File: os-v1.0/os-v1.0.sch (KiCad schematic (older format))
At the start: 53 parts, among them J1 Conn_01x02, J2 Conn_01x04, Q1 2N7002, SW1 SW_Push, SW2 SW_Push, SW3 SW_Push, SW4 SW_Push, SW5 SW_Push, U1 DS3231MZ, U10 MCP1812AT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

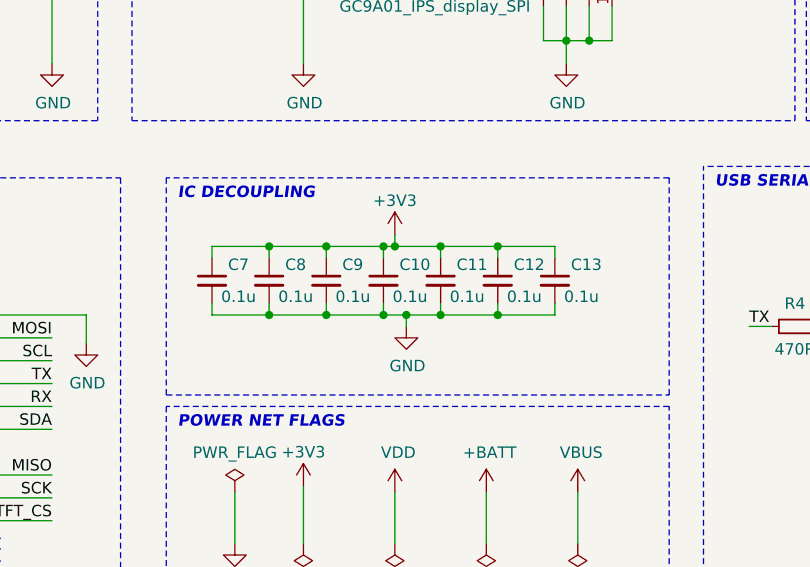
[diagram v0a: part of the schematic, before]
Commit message: adds addl cap to ch240e and updates board and bom
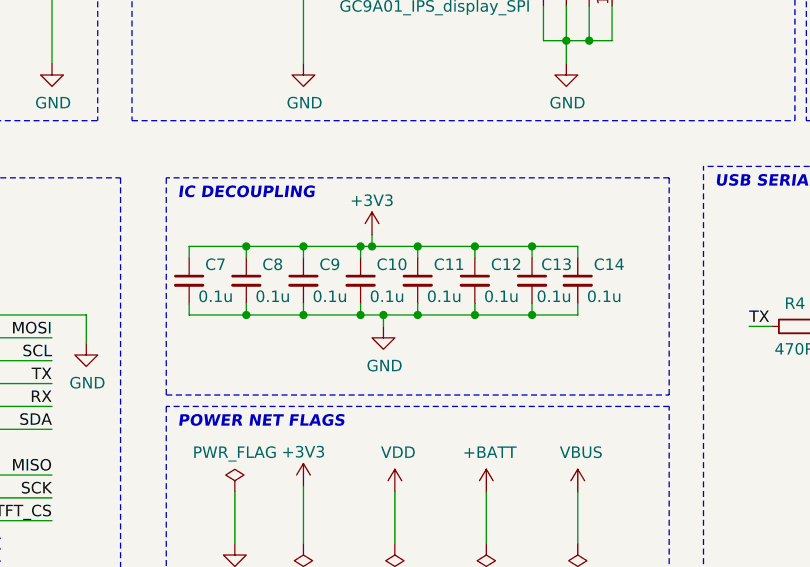
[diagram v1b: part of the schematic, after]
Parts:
- added C14: 0.1u, Capacitor_SMD:C_0603_1608Metric, symbol Device:C_Small
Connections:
- net +3V3: now also C14.1
- net GND: now also C14.2
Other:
- moved on the sheet: C10, C11, C12, C13, C7, C8, C9
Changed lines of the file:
@@
 Comment1 ""
 Comment2 ""
-Comment3 "Add 0.1u decoupling capacitor to Vcc/Vdd for U1-U3,U6"
+Comment3 "Add 0.1u decoupling capacitor to each Vcc/Vdd pin on U1-U3,U6"
 Comment4 "All resistors and capacitors are 0603 unless otherwise noted"
 $EndDescr
@@
 L power:GND #PWR057
 U 1 1 5F641A31
-P 6850 3350
-F 0 "#PWR057" H 6850 3100 50  0001 C CNN
-F 1 "GND" H 6855 3177 50  0000 C CNN
-F 2 "" H 6850 3350 50  0001 C CNN
-F 3 "" H 6850 3350 50  0001 C CNN
-	1    6850 3350
+P 6750 3350
+F 0 "#PWR057" H 6750 3100 50  0001 C CNN
+F 1 "GND" H 6755 3177 50  0000 C CNN
+F 2 "" H 6750 3350 50  0001 C CNN
+F 3 "" H 6750 3350 50  0001 C CNN
+	1    6750 3350
 	1    0    0    -1
 $EndComp
@@
 L Device:C_Small C9
 U 1 1 5F753E14
-P 6500 3150
-F 0 "C9" H 6570 3220 50  0000 L CNN
-F 1 "0.1u" H 6540 3080 50  0000 L CNN
-F 2 "Capacitor_SMD:C_0603_1608Metric" H 6500 3150 50  0001 C CNN
-F 3 "~" H 6500 3150 50  0001 C CNN
-	1    6500 3150
+P 6400 3150
+F 0 "C9" H 6470 3220 50  0000 L CNN
+F 1 "0.1u" H 6440 3080 50  0000 L CNN
+F 2 "Capacitor_SMD:C_0603_1608Metric" H 6400 3150 50  0001 C CNN
+F 3 "~" H 6400 3150 50  0001 C CNN
+	1    6400 3150
 	1    0    0    -1
 $EndComp
@@
 L Device:C_Small C10
 U 1 1 5F827434
-P 6750 3150
-F 0 "C10" H 6820 3220 50  0000 L CNN
-F 1 "0.1u" H 6790 3080 50  0000 L CNN
-F 2 "Capacitor_SMD:C_0603_1608Metric" H 6750 3150 50  0001 C CNN
-F 3 "~" H 6750 3150 50  0001 C CNN
-	1    6750 3150
+P 6650 3150
+F 0 "C10" H 6720 3220 50  0000 L CNN
+F 1 "0.1u" H 6690 3080 50  0000 L CNN
+F 2 "Capacitor_SMD:C_0603_1608Metric" H 6650 3150 50  0001 C CNN
+F 3 "~" H 6650 3150 50  0001 C CNN
+	1    6650 3150
 	1    0    0    -1
 $EndComp
@@
 L Device:C_Small C11
 U 1 1 5F8276CE
-P 7000 3150
-F 0 "C11" H 7070 3220 50  0000 L CNN
-F 1 "0.1u" H 7040 3080 50  0000 L CNN
-F 2 "Capacitor_SMD:C_0603_1608Metric" H 7000 3150 50  0001 C CNN
-F 3 "~" H 7000 3150 50  0001 C CNN
-	1    7000 3150
+P 6900 3150
+F 0 "C11" H 6970 3220 50  0000 L CNN
+F 1 "0.1u" H 6940 3080 50  0000 L CNN
+F 2 "Capacitor_SMD:C_0603_1608Metric" H 6900 3150 50  0001 C CNN
+F 3 "~" H 6900 3150 50  0001 C CNN
+	1    6900 3150
 	1    0    0    -1
 $EndComp
@@
 L Device:C_Small C12
 U 1 1 5F828FE0
-P 7250 3150
-F 0 "C12" H 7320 3220 50  0000 L CNN
-F 1 "0.1u" H 7290 3080 50  0000 L CNN
-F 2 "Capacitor_SMD:C_0603_1608Metric" H 7250 3150 50  0001 C CNN
-F 3 "~" H 7250 3150 50  0001 C CNN
-	1    7250 3150
+P 7150 3150
+F 0 "C12" H 7220 3220 50  0000 L CNN
+F 1 "0.1u" H 7190 3080 50  0000 L CNN
+F 2 "Capacitor_SMD:C_0603_1608Metric" H 7150 3150 50  0001 C CNN
+F 3 "~" H 7150 3150 50  0001 C CNN
+	1    7150 3150
 	1    0    0    -1
 $EndComp
@@
 L Device:C_Small C13
 U 1 1 5F8293A4
-P 7500 3150
-F 0 "C13" H 7570 3220 50  0000 L CNN
-F 1 "0.1u" H 7540 3080 50  0000 L CNN
-F 2 "Capacitor_SMD:C_0603_1608Metric" H 7500 3150 50  0001 C CNN
-F 3 "~" H 7500 3150 50  0001 C CNN
-	1    7500 3150
+P 7400 3150
+F 0 "C13" H 7440 3220 50  0000 L CNN
+F 1 "0.1u" H 7420 3080 50  0000 L CNN
+F 2 "Capacitor_SMD:C_0603_1608Metric" H 7400 3150 50  0001 C CNN
+F 3 "~" H 7400 3150 50  0001 C CNN
+	1    7400 3150
 	1    0    0    -1
 $EndComp
@@
 L Device:C_Small C8
 U 1 1 5F82A290
-P 6250 3150
-F 0 "C8" H 6320 3220 50  0000 L CNN
-F 1 "0.1u" H 6290 3080 50  0000 L CNN
-F 2 "Capacitor_SMD:C_0603_1608Metric" H 6250 3150 50  0001 C CNN
-F 3 "~" H 6250 3150 50  0001 C CNN
-	1    6250 3150
+P 6150 3150
+F 0 "C8" H 6220 3220 50  0000 L CNN
+F 1 "0.1u" H 6190 3080 50  0000 L CNN
+F 2 "Capacitor_SMD:C_0603_1608Metric" H 6150 3150 50  0001 C CNN
+F 3 "~" H 6150 3150 50  0001 C CNN
+	1    6150 3150
 	1    0    0    -1
 $EndComp
@@
 L Device:C_Small C7
 U 1 1 5F82A534
-P 6000 3150
-F 0 "C7" H 6070 3220 50  0000 L CNN
-F 1 "0.1u" H 6040 3080 50  0000 L CNN
-F 2 "Capacitor_SMD:C_0603_1608Metric" H 6000 3150 50  0001 C CNN
-F 3 "~" H 6000 3150 50  0001 C CNN
-	1    6000 3150
+P 5900 3150
+F 0 "C7" H 5970 3220 50  0000 L CNN
+F 1 "0.1u" H 5940 3080 50  0000 L CNN
+F 2 "Capacitor_SMD:C_0603_1608Metric" H 5900 3150 50  0001 C CNN
+F 3 "~" H 5900 3150 50  0001 C CNN
+	1    5900 3150
 	1    0    0    -1
 $EndComp
@@
 L power:+3V3 #PWR056
 U 1 1 5F890CE1
-P 6800 2950
-F 0 "#PWR056" H 6800 2800 50  0001 C CNN
-F 1 "+3V3" H 6800 3100 50  0000 C CNN
-F 2 "" H 6800 2950 50  0001 C CNN
-F 3 "" H 6800 2950 50  0001 C CNN
-	1    6800 2950
+P 6700 2950
+F 0 "#PWR056" H 6700 2800 50  0001 C CNN
+F 1 "+3V3" H 6700 3100 50  0000 C CNN
+F 2 "" H 6700 2950 50  0001 C CNN
+F 3 "" H 6700 2950 50  0001 C CNN
+	1    6700 2950
 	1    0    0    -1
 $EndComp
@@
 $EndComp
 Wire Wire Line
-	6000 3250 6000 3300
-Wire Wire Line
-	6000 3300 6250 3300
-Wire Wire Line
-	6250 3300 6250 3250
-Wire Wire Line
-	6250 3300 6500 3300
-Wire Wire Line
-	6500 3300 6500 3250
-Connection ~ 6250 3300
-Wire Wire Line
-	6500 3300 6750 3300
-Connection ~ 6500 3300
-Connection ~ 6850 3300
-Wire Wire Line
-	6850 3300 6850 3350
-Wire Wire Line
-	6850 3300 7000 3300
-Wire Wire Line
-	7000 3300 7000 3250
-Wire Wire Line
-	7000 3300 7250 3300
-Wire Wire Line
-	7250 3300 7250 3250
-Connection ~ 7000 3300
-Wire Wire Line
-	7250 3300 7500 3300
-Wire Wire Line
-	7500 3300 7500 3250
-Connection ~ 7250 3300
-Wire Wire Line
-	7500 3050 7500 3000
-Wire Wire Line
-	7500 3000 7250 3000
-Wire Wire Line
-	7250 3000 7250 3050
-Wire Wire Line
-	7250 3000 7000 3000
-Wire Wire Line
-	7000 3000 7000 3050
-Connection ~ 7250 3000
-Wire Wire Line
-	7000 3000 6800 3000
-Wire Wire Line
-	6750 3000 6750 3050
-Connection ~ 7000 3000
-Wire Wire Line
-	6800 3000 6800 2950
-Connection ~ 6800 3000
-Wire Wire Line
-	6800 3000 6750 3000
-Wire Wire Line
-	6250 3050 6250 3000
-Wire Wire Line
-	6250 3000 6500 3000
-Wire Wire Line
-	6500 3000 6500 3050
-Wire Wire Line
-	6500 3000 6750 3000
-Connection ~ 6500 3000
-Connection ~ 6750 3000
-Wire Wire Line
-	6250 3000 6000 3000
-Wire Wire Line
-	6000 3000 6000 3050
-Connection ~ 6250 3000
+	5900 3250 5900 3300
+Wire Wire Line
+	5900 3300 6150 3300
+Wire Wire Line
+	6150 3300 6150 3250
+Wire Wire Line
+	6150 3300 6400 3300
+Wire Wire Line
+	6400 3300 6400 3250
+Connection ~ 6150 3300
+Wire Wire Line
+	6400 3300 6650 3300
+Connection ~ 6400 3300
+Connection ~ 6750 3300
+Wire Wire Line
+	6750 3300 6750 3350
+Wire Wire Line
+	6750 3300 6900 3300
+Wire Wire Line
+	6900 3300 6900 3250
+Wire Wire Line
+	6900 3300 7150 3300
+Wire Wire Line
+	7150 3300 7150 3250
+Connection ~ 6900 3300
+Wire Wire Line
+	7150 3300 7400 3300
+Wire Wire Line
+	7400 3300 7400 3250
+Connection ~ 7150 3300
+Wire Wire Line
+	7400 3050 7400 3000
+Wire Wire Line
+	7400 3000 7150 3000
+Wire Wire Line
+	7150 3000 7150 3050
+Wire Wire Line
+	7150 3000 6900 3000
+Wire Wire Line
+	6900 3000 6900 3050
+Connection ~ 7150 3000
+Wire Wire Line
+	6900 3000 6700 3000
+Wire Wire Line
+	6650 3000 6650 3050
+Connection ~ 6900 3000
+Wire Wire Line
+	6700 3000 6700 2950
+Connection ~ 6700 3000
+Wire Wire Line
+	6700 3000 6650 3000
+Wire Wire Line
+	6150 3050 6150 3000
+Wire Wire Line
+	6150 3000 6400 3000
+Wire Wire Line
+	6400 3000 6400 3050
+Wire Wire Line
+	6400 3000 6650 3000
+Connection ~ 6400 3000
+Connection ~ 6650 3000
+Wire Wire Line
+	6150 3000 5900 3000
+Wire Wire Line
+	5900 3000 5900 3050
+Connection ~ 6150 3000
 $Comp
 L power:PWR_FLAG #FLG02
@@
 	7600 4300 7600 4075
 Wire Wire Line
-	6750 3250 6750 3300
-Connection ~ 6750 3300
-Wire Wire Line
-	6750 3300 6850 3300
+	6650 3250 6650 3300
+Connection ~ 6650 3300
+Wire Wire Line
+	6650 3300 6750 3300
 Wire Notes Line
 	5800 2700 5800 3650
@@
 Wire Wire Line
 	2000 6450 2000 6500
+$Comp
+L Device:C_Small C14
+U 1 1 5FB79A24
+P 7600 3150
+F 0 "C14" H 7670 3220 50  0000 L CNN
+F 1 "0.1u" H 7640 3080 50  0000 L CNN
+F 2 "Capacitor_SMD:C_0603_1608Metric" H 7600 3150 50  0001 C CNN
+F 3 "~" H 7600 3150 50  0001 C CNN
+	1    7600 3150
+	1    0    0    -1
+$EndComp
+Wire Wire Line
+	7400 3000 7600 3000
+Wire Wire Line
+	7600 3000 7600 3050
+Connection ~ 7400 3000
+Wire Wire Line
+	7600 3250 7600 3300
+Wire Wire Line
+	7600 3300 7400 3300
+Connection ~ 7400 3300
 $EndSCHEMATC
